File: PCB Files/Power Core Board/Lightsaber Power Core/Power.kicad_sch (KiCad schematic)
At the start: 44 parts

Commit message: Checkpoint before removing VEXT switches
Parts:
- R?: value R_US -> 10k
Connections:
- net VEXT: now also U?.4 (VP)
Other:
- moved on the sheet: C?, D?, R?, U?

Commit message: Schematic drawn, ready for post-wiring
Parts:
- removed C? (x2): 10uF, symbol Device:C
- removed D?: D_Schottky_Filled, symbol Device:D_Schottky_Filled
- removed J?: JST PH, symbol Connector_Generic:Conn_01x02
- removed J?: USB-C, symbol Connector:USB_C_Receptacle_USB2.0_16P
- removed Q? (x2): 2302V, symbol Device:Q_NMOS_GSD
- removed Q? (x2): AO3401A, symbol Device:Q_PMOS_GSD
- removed R? (x4): 10k, symbol Device:R_US
- removed R? (x2): 5.1k, symbol Device:R_US
- removed R?: 1k, symbol Device:R_US
- removed U?: CM1213A−02Sx, symbol irex_Power_Protection:CM1213A−02Sx
- L?: value 2.2uH -> 1.0uH; footprint Inductor_SMD:L_Bourns_SRP7028A_7.3x6.6mm -> irex_Inductor_SMD:L_0806_2016Metric; LCSC PN (none) -> C161082; MPN (none) -> DFE201610E-1R0M; Saturation Current 10A -> 3.6A
- R?: value 107k -> 10k
- R?: value 357k -> 32.4k
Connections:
- net 5.0V_EN: now also R?.2, U?.2 (EN)
- net GND: now also R?.1
- net VBAT: now also C?.1, C?.1, C?.1, L?.1, R?.2, U?.1 (IN), U?.4 (VIN)
- net VEXT renamed VBUS
- removed net VSYS: C?.1, C?.1, C?.1, L?.1, R?.2, R?.2, U?.1 (IN), U?.4 (VIN)
- no-connect marks 2 -> 0
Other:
- note added: "Power"
- note removed: "Input Power Muxing"
- note removed: "USB Input"
- moved on the sheet: C?, D?, L?, R?, U?

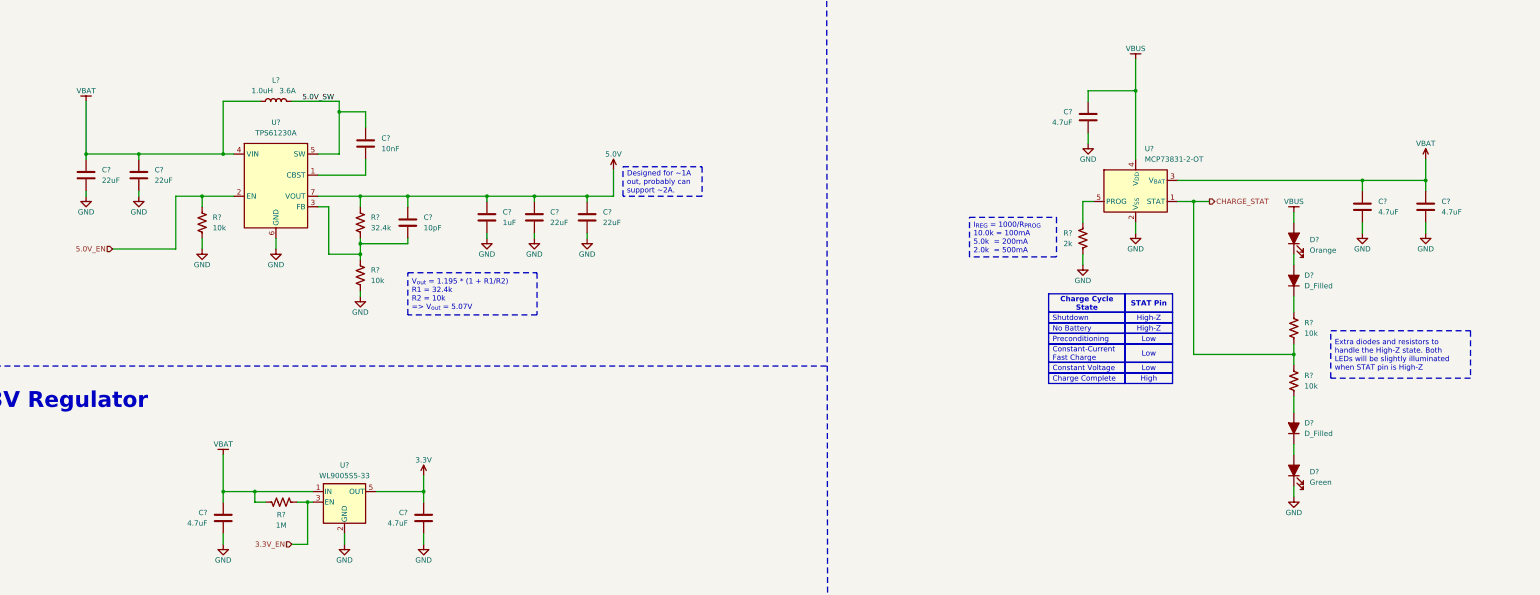
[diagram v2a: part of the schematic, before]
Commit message: Added BOM parts, need to make new library part for LED
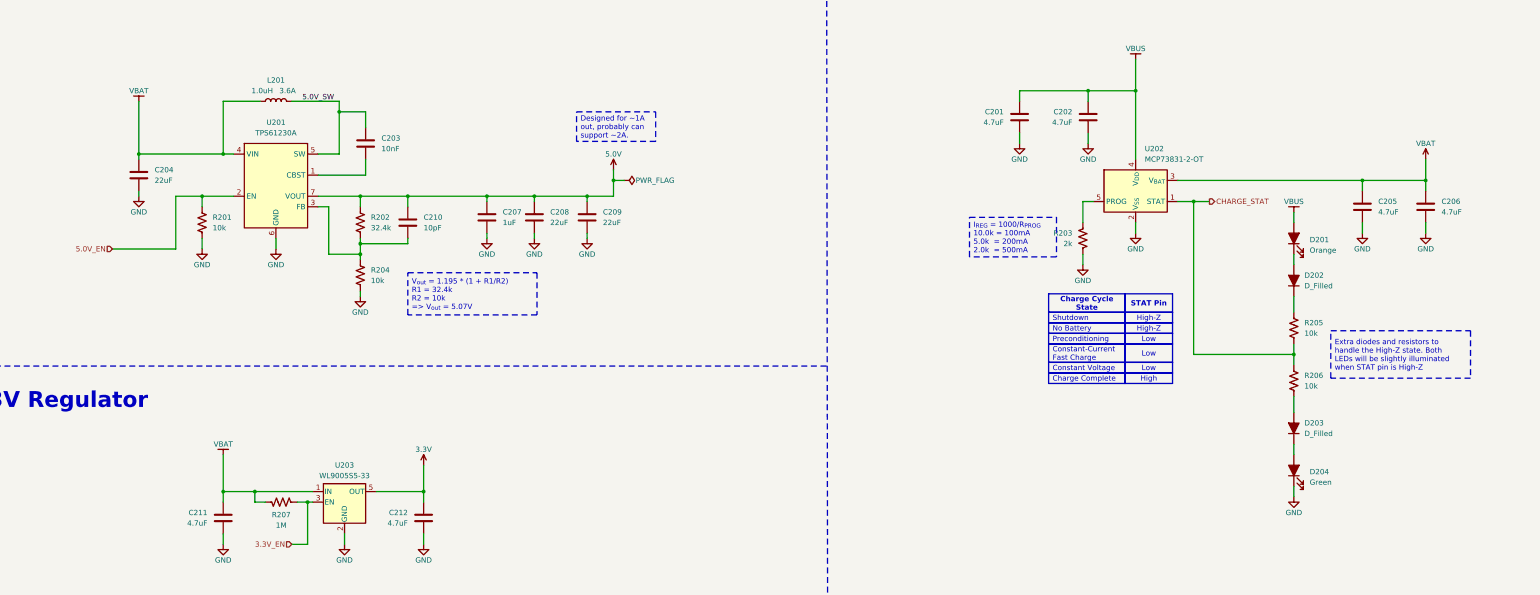
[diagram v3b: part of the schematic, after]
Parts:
- removed C?: 22uF, symbol Device:C
- added C201: 4.7uF, Capacitor_SMD:C_0603_1608Metric, symbol Device:C
- C202, C205, C206, C211, C212: renamed from C?; footprint (none) -> Capacitor_SMD:C_0603_1608Metric; LCSC PN (none) -> C1705; MPN (none) -> CL10A475KP8NNNC
- C203: renamed from C?; footprint (none) -> Capacitor_SMD:C_0402_1005Metric; LCSC PN (none) -> C15195; MPN (none) -> CL05B103KB5NNNC
- C204, C208, C209: renamed from C?; footprint (none) -> Capacitor_SMD:C_0603_1608Metric; LCSC PN (none) -> C2762594; MPN (none) -> CL10A226MO7JZNC
- C207: renamed from C?; footprint (none) -> Capacitor_SMD:C_0402_1005Metric; LCSC PN (none) -> C14445; MPN (none) -> CL05A105KP5NNNC
- C210: renamed from C?; footprint (none) -> Capacitor_SMD:C_0402_1005Metric; LCSC PN (none) -> C76946; MPN (none) -> GRM1555C1H100JA01D
- D201: renamed from D?; LCSC PN (none) -> C965845; MPN (none) -> XL-2012SURUGC
- D202, D203: renamed from D?; footprint (none) -> Diode_SMD:D_SOD-523; LCSC PN (none) -> C282366; MPN (none) -> BAS716,115
- R201, R204, R205, R206: renamed from R?; footprint (none) -> Resistor_SMD:R_0402_1005Metric; LCSC PN (none) -> C60490; MPN (none) -> RC0402FR-0710KL
- R202: renamed from R?; footprint (none) -> Resistor_SMD:R_0402_1005Metric; LCSC PN (none) -> C852723; MPN (none) -> RT0402BRD0732K4L
- R203: renamed from R?; footprint (none) -> Resistor_SMD:R_0402_1005Metric; LCSC PN (none) -> C60488; MPN (none) -> RC0402FR-072KL
- R207: renamed from R?; footprint (none) -> Resistor_SMD:R_0402_1005Metric; LCSC PN (none) -> C93949; MPN (none) -> RC0402JR-071ML
- U201: renamed from U?; LCSC PN (none) -> C376005; MPN (none) -> TPS61230ARNSR
- U202: renamed from U?; LCSC PN (none) -> C424093; MPN (none) -> MCP73831T-2ACI/OT
- U203: renamed from U?; LCSC PN (none) -> C2688249; MPN (none) -> WL9005S5-33
- gave numbers to parts that had none: 2
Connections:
- net GND: now also C201.2
- net VBUS: now also C201.1

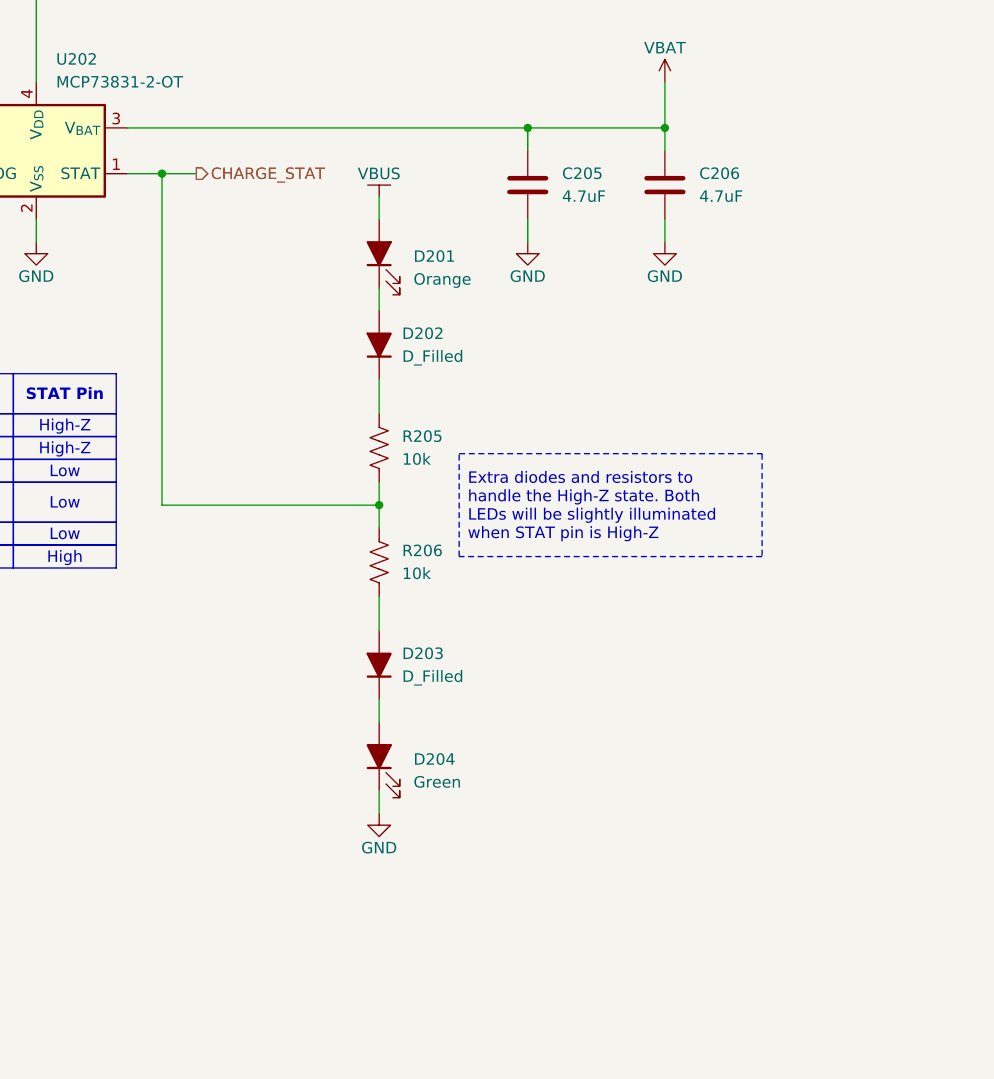
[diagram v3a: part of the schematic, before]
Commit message: Schematic finished, ready for layout
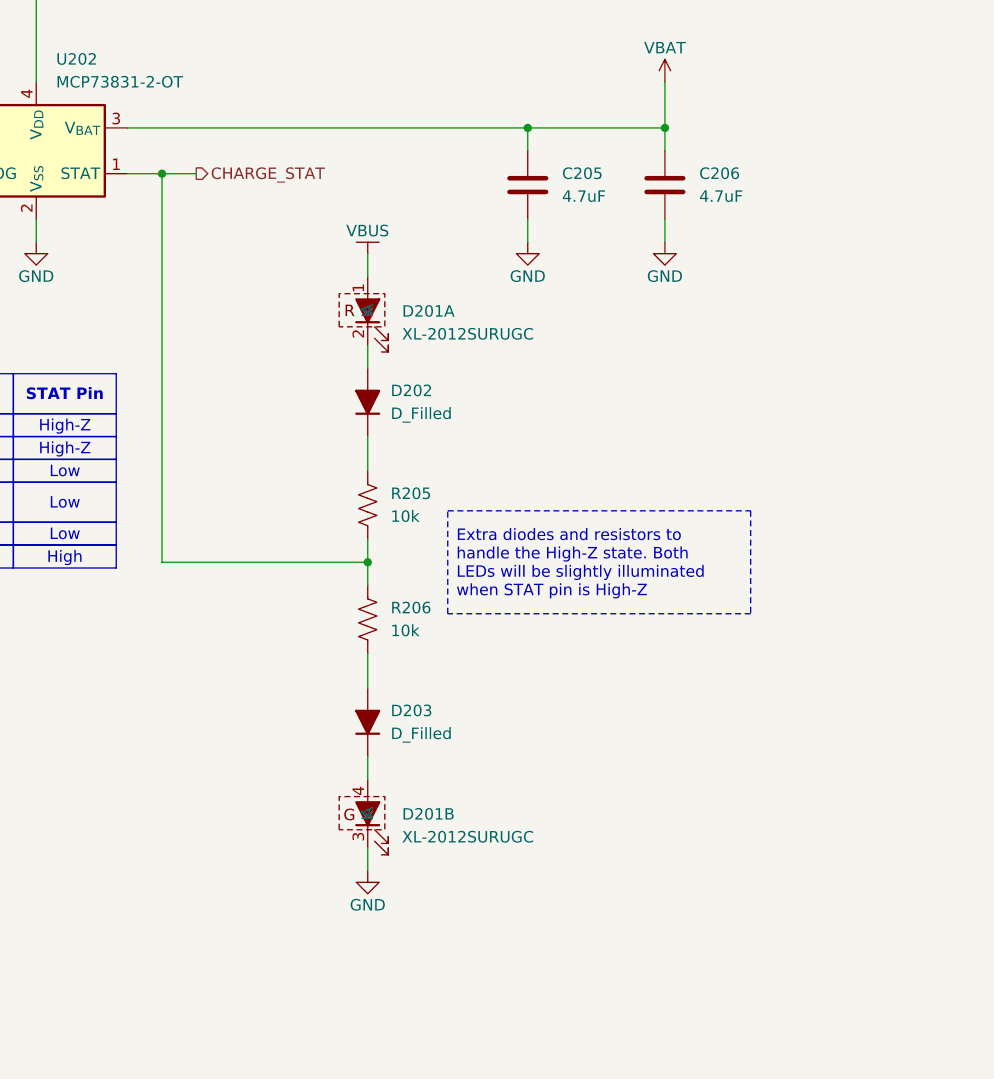
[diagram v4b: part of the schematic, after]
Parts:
- removed D201: Orange, symbol Device:LED_Filled
- removed D204: Green, symbol Device:LED_Filled
- added D201: XL-2012SURUGC, Package_TO_SOT_SMD:SOT-23, symbol irex_LED:LED_RG_XINGLIGHT_XL-2012SURUGC
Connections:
- net GND: now also D201.3 (K)
- net VBUS: now also D201.1 (A)
- net at D203.1 (K): now also D201.4 (A)
- net at D202.2 (A): now also D201.2 (K)
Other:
- moved on the sheet: D202, D203, R205, R206
